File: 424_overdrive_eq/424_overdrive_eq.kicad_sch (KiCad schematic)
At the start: 11 parts, among them U1 Opamp_Dual

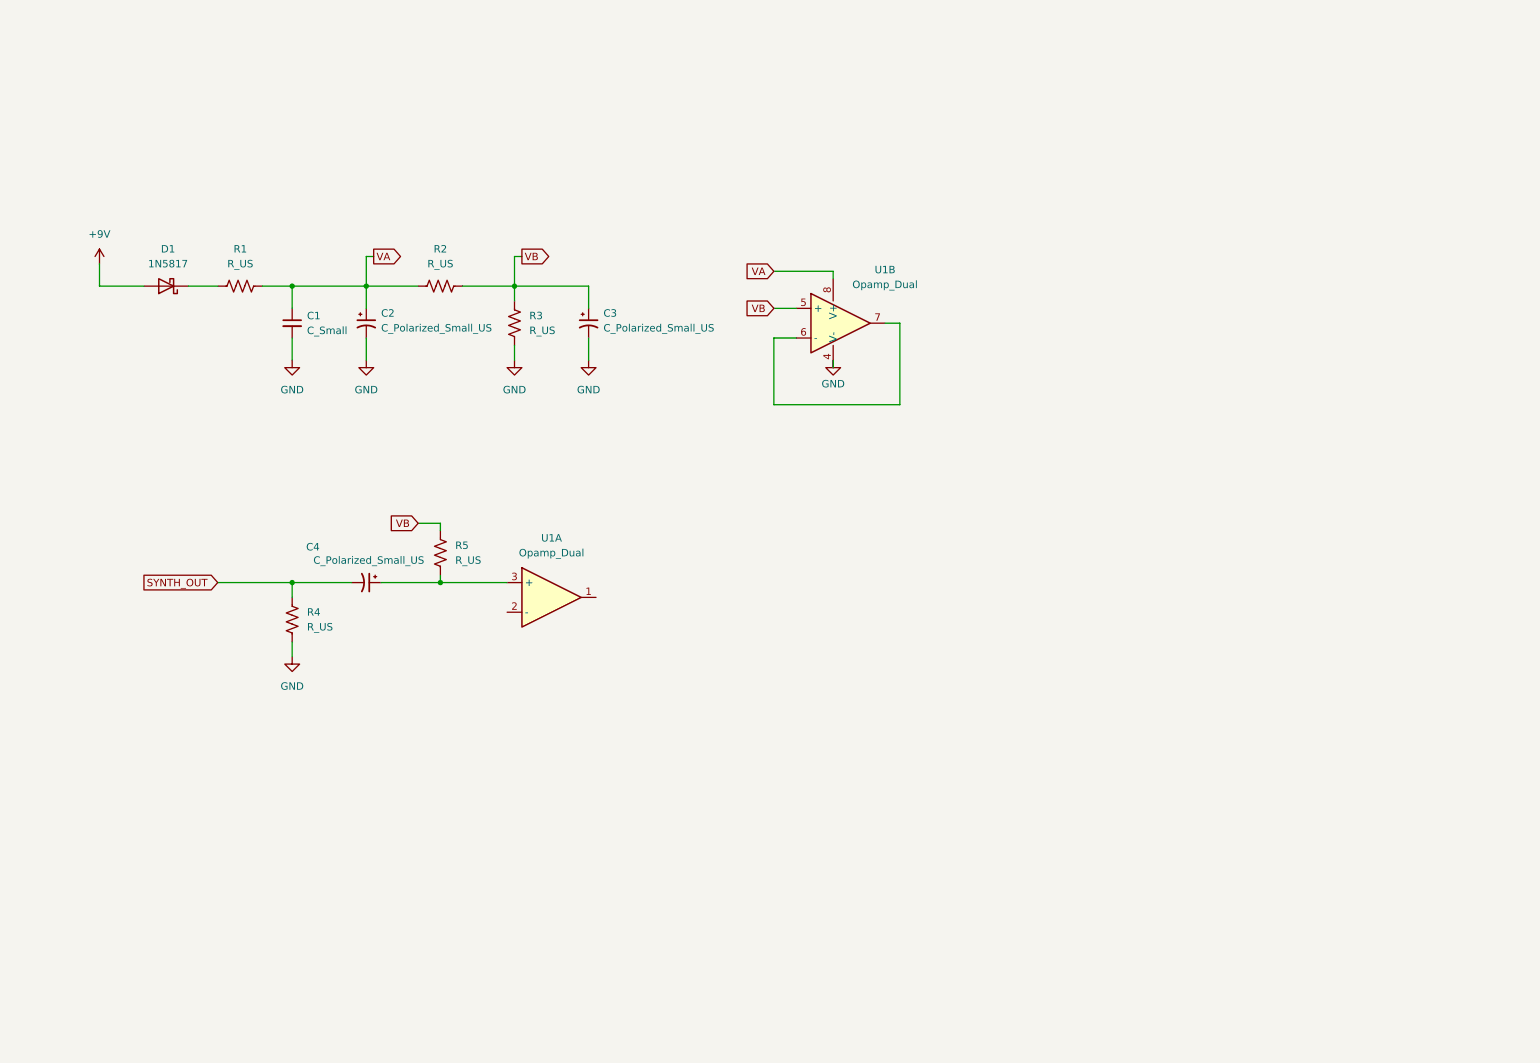
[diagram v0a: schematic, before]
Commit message: completed 424 kicad schematic
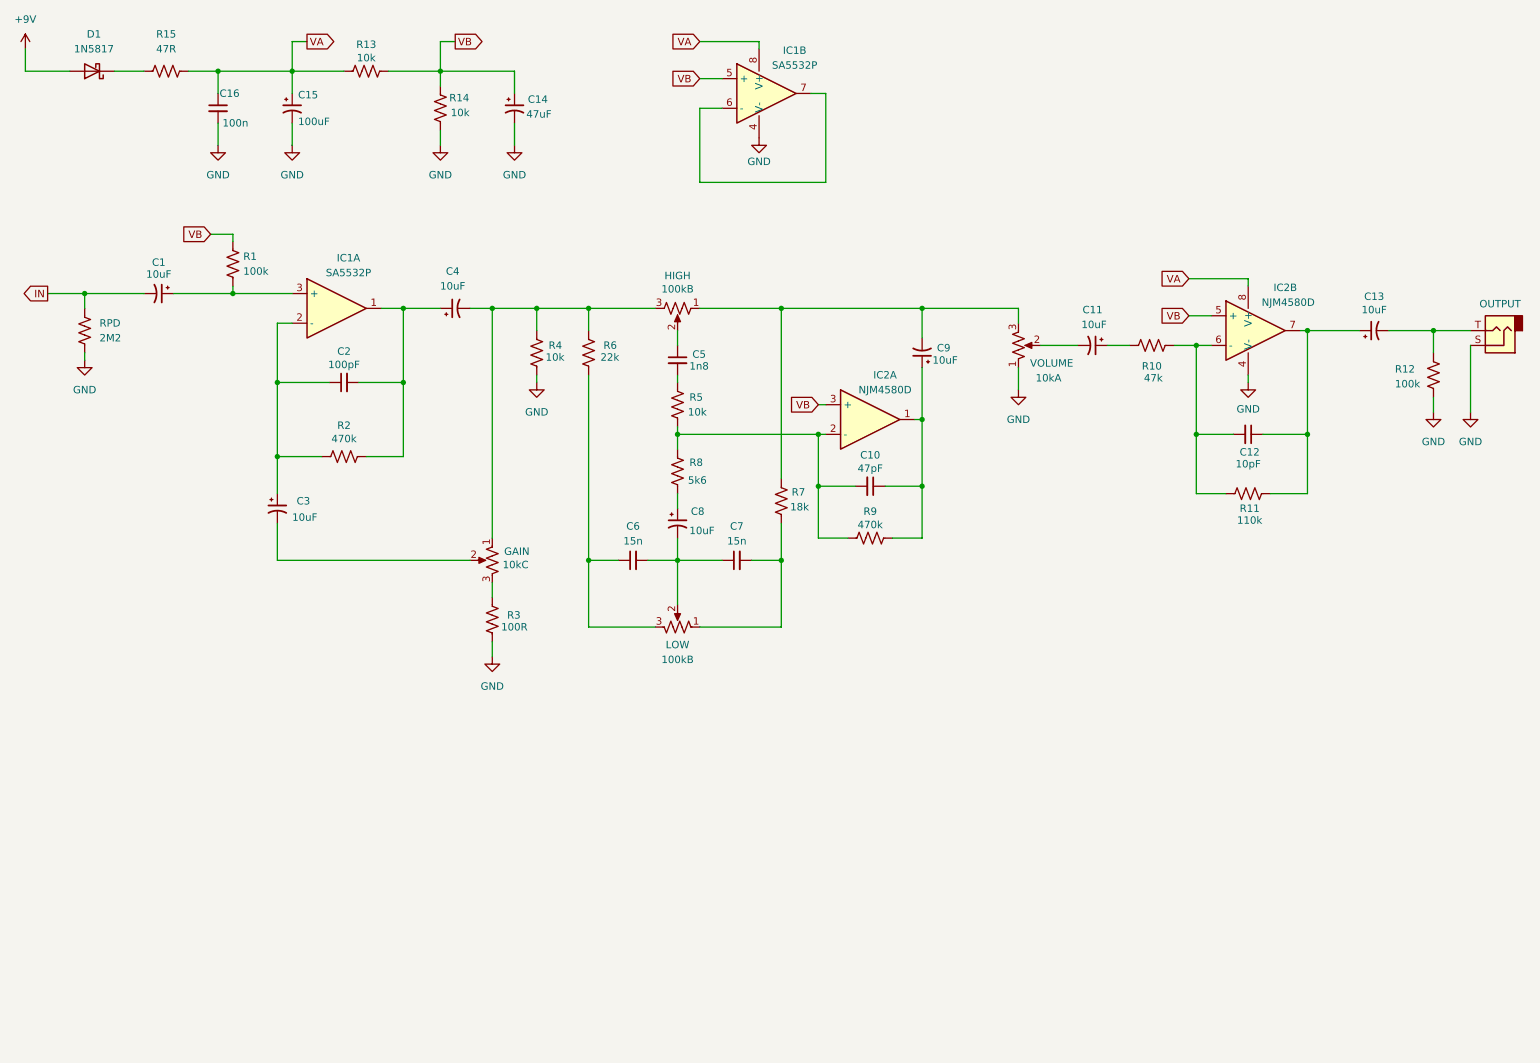
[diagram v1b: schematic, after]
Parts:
- added 100kB: LOW, symbol Device:R_Potentiometer_US
- added C10: 47pF, symbol Device:C_Small
- added C11, C13, C3, C4, C8, C9: 10uF, symbol Device:C_Polarized_Small_US
- added C12: 10pF, symbol Device:C_Small
- added C2: 100pF, symbol Device:C_Small
- added C5: 1n8, symbol Device:C_Small
- added C6, C7: 15n, symbol Device:C_Small
- added GAIN: 10kC, symbol Device:R_Potentiometer_US
- added HIGH: 100kB, symbol Device:R_Potentiometer_US
- added IC2: NJM4580D, symbol Device:Opamp_Dual
- added J1: OUTPUT, symbol Connector_Audio:AudioJack2
- added R10: 47k, symbol Device:R_US
- added R11: 110k, symbol Device:R_US
- added R12: 100k, symbol Device:R_US
- added R2, R9: 470k, symbol Device:R_US
- added R3: 100R, symbol Device:R_US
- added R4, R5: 10k, symbol Device:R_US
- added R6: 22k, symbol Device:R_US
- added R7: 18k, symbol Device:R_US
- added R8: 5k6, symbol Device:R_US
- added U2: Opamp_Dual, symbol Device:Opamp_Dual
- added VOLUME: 10kA, symbol Device:R_Potentiometer_US
- C1: renamed from C4; value C_Polarized_Small_US -> 10uF
- C14: renamed from C3; value C_Polarized_Small_US -> 47uF
- C15: renamed from C2; value C_Polarized_Small_US -> 100uF
- C16: renamed from C1; value C_Small -> 100n
- IC1: renamed from U1; value Opamp_Dual -> SA5532P
- R1: renamed from R5; value R_US -> 100k
- R13: renamed from R2; value R_US -> 10k
- R14: renamed from R3; value R_US -> 10k
- R15: renamed from R1; value R_US -> 47R
- RPD: renamed from R4; value R_US -> 2M2
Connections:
- net GND: now also J1.S, R12.2, R3.2, R4.2, U2.4 (V-), VOLUME.1
- net VA: now also U2.8 (V+)
- net VB: now also IC2.3 (+), IC2.5 (+)
- net IN: now reaches C1.2, RPD.1
- net at IC1.1: now also C2.2, C4.1, R2.2
- net at IC1.2 (-): now also C2.1, C3.1, R2.1
- new net: C4.2, GAIN.1, HIGH.3, R4.1, R6.1
- new net: C3.2, GAIN.2
- new net: GAIN.3, R3.1
- new net: C10.1, C9.1, IC2.1, R9.1
- new net: C10.2, IC2.2 (-), R5.2, R8.1, R9.2
- new net: C11.2, VOLUME.2
- new net: C9.2, HIGH.1, R7.1, VOLUME.3
- new net: C12.2, IC2.6 (-), R10.1, R11.2
- new net: C12.1, C13.1, IC2.7, R11.1
- new net: C11.1, R10.2
- new net: C8.1, R8.2
- new net: 100kB.2, C6.2, C7.1, C8.2
- new net: C13.2, J1.T, R12.1
- new net: 100kB.3, C6.1, R6.2
- new net: 100kB.1, C7.2, R7.2
- new net: C5.2, R5.1
- new net: C5.1, HIGH.2
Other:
- moved on the sheet: C1, C14, C15, C16, D1, IC1A, IC1B, R1, R13, R14, R15, RPD

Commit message: added notes
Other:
- note added: "03/13/2026"
- note added: "424 PREAMP OVERDRIVE / EQ"
- note added: "Note: Adapted from AionFX 424 Tape Preamp circuit, itself adapted from the TASCAM 424 Portastudio"
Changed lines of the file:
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@@
 	(generator_version "9.0")
 	(paper "A4")
+	(text "03/13/2026\n"
+		(exclude_from_sim no)
+		(at 212.598 193.548 0)
+		(effects
+			(font
+				(size 1.27 1.27)
+				(color 132 0 0 1)
+			)
+		)
+	)
+	(text "424 PREAMP OVERDRIVE / EQ"
+		(exclude_from_sim no)
+		(at 201.422 189.738 0)
+		(effects
+			(font
+				(size 1.27 1.27)
+				(color 132 0 0 1)
+			)
+		)
+	)
+	(text "Note: Adapted from AionFX 424 Tape Preamp circuit, itself adapted from the TASCAM 424 Portastudio"
+		(exclude_from_sim no)
+		(at 225.552 168.656 0)
+		(effects
+			(font
+				(size 1.016 1.016)
+				(color 132 0 0 1)
+			)
+		)
+	)
 	(junction
 		(at 82.55 67.31)
